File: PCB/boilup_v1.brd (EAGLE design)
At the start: 46.7 x 80 mm, 38 parts, among them IC1 THS4211, J1 USB-MICROB, U1 STM32F0_LQFP64, U2 SPX3819-3.3

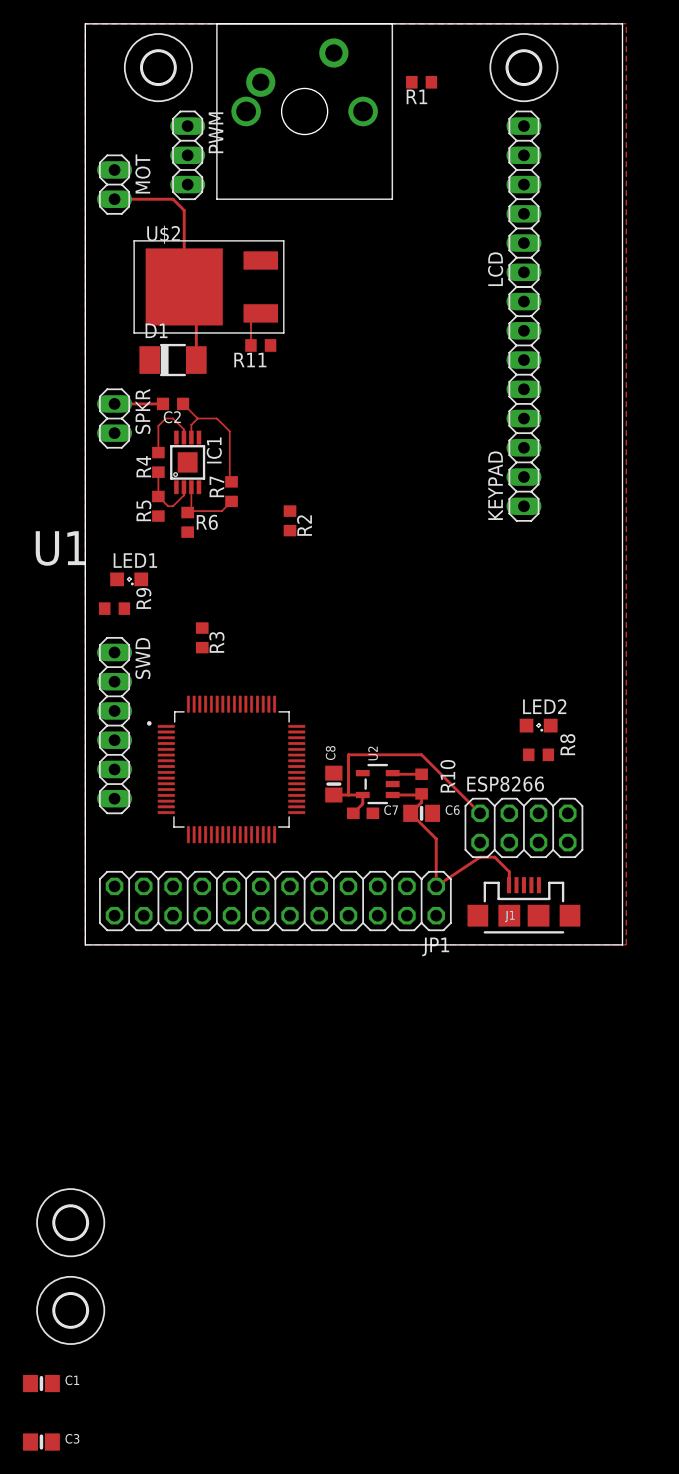
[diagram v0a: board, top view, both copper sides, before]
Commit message: Initial routing + pinout
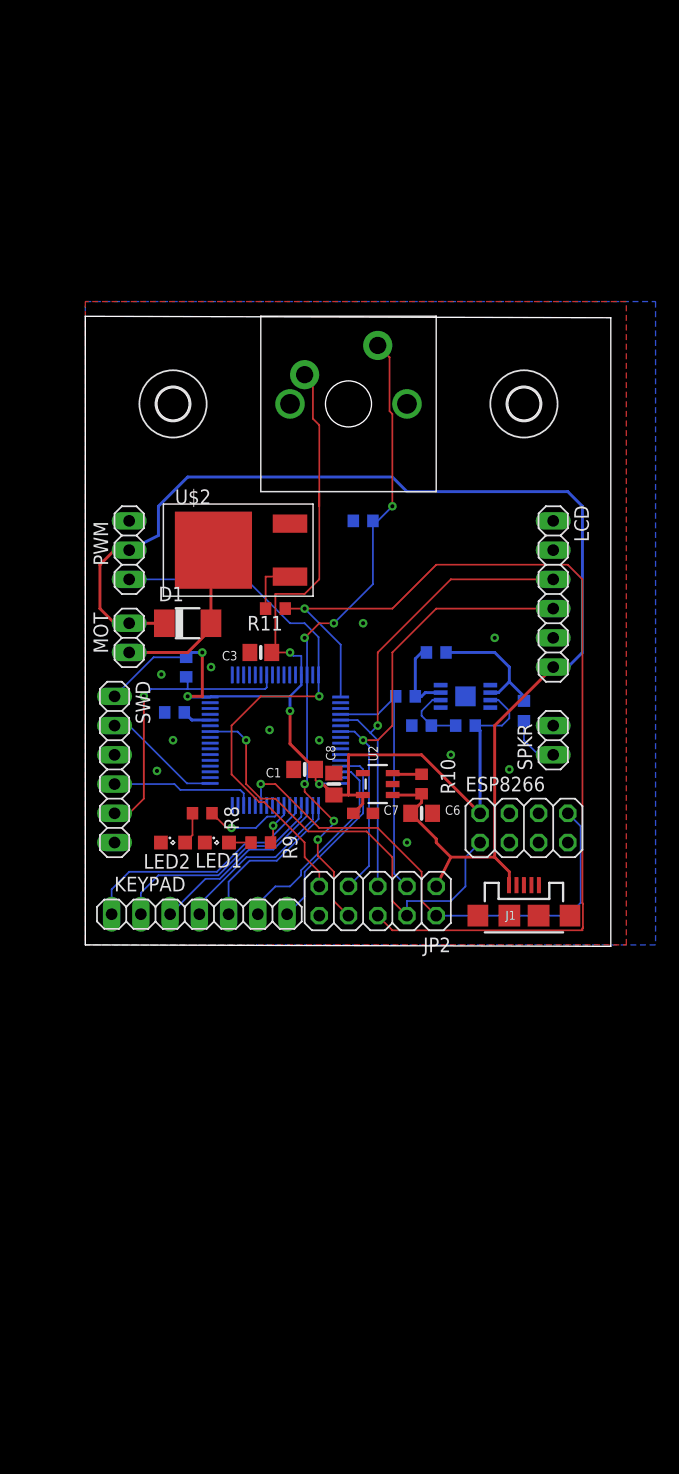
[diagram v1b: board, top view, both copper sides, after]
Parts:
- removed H3, H4: MOUNT-HOLE2.8, holes:2,8
- removed JP1: (no value), pinhead:2X12
- added JP2: (no value), pinhead:2X05
- KEYPAD: device pinhead:1X08 -> pinhead:1X07
- moved C3 71.2 mm to (15.2, 25.4), turned to 180 degrees
- moved C1 58.0 mm to (19.1, 15.2), turned to 180 degrees
- moved KEYPAD 52.5 mm to (9.91, 2.67), turned to 180 degrees
- moved SPKR 47.2 mm to (40.6, 17.8), turned to 90 degrees
- moved C2 40.5 mm to (38.1, 20.3), flipped to the bottom, turned to 270 degrees
- moved MOT 39.4 mm to (3.81, 26.7)
- moved R1 38.4 mm to (24.1, 36.8), flipped to the bottom
- moved R4 35.1 mm to (33.0, 19.1), flipped to the bottom, turned to 0 degrees
- moved PWM 34.7 mm to (3.81, 34.3)
- moved LCD 34.4 mm to (40.6, 30.5), turned to 270 degrees
- moved LED2 33.3 mm to (7.62, 8.89), turned to 0 degrees
- moved IC1 31.5 mm to (33.0, 21.6), flipped to the bottom, turned to 90 degrees
- moved R5 29.8 mm to (29.2, 19.1), flipped to the bottom, turned to 0 degrees
- moved R8 29.6 mm to (10.2, 11.4)
- moved H2 29.2 mm to (7.62, 47.0)
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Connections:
- removed net KETTLESWITCH: R1.2, U$1.SW2
- removed net N$22: JP1.22
- removed net N$23: JP1.20
- net +5V: now also JP2.1; no longer JP1.1
- net COL1: no longer JP1.11
- net COL2: no longer JP1.13
- net COL3: no longer JP1.15
- net DAC: now also JP2.3; no longer JP1.17
- net GND: now also JP2.10; no longer JP1.24
- net LED3: no longer JP1.12
- net LED4: no longer JP1.14
- net MISO: no longer JP1.21
- net MOSI: now also JP2.7; no longer JP1.23
- net PUSH_BUTT: now also JP2.8, R1.2, U$1.SW2; no longer JP1.10
- net ROW1: no longer JP1.3
- net ROW2: no longer JP1.5
- net ROW3: no longer JP1.7
- net ROW4: no longer JP1.9
- net SCK: now also JP2.5; no longer JP1.19
- net SWCLK: no longer JP1.18
- net SWDIO: no longer JP1.16
- net TIM2_CH3: now also JP2.9; no longer JP1.6
- net TIM2_CH4: now also JP2.6; no longer JP1.8
- net USART_RX: now also JP2.2; no longer JP1.2
- net USART_TX: now also JP2.4; no longer JP1.4
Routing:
- net +5V: track 20.7 -> 111.2 mm
- net TIM2_CH4: track 0.00 -> 85.7 mm, vias 0 -> 1
- net +3V3: track 27.4 -> 106.3 mm, vias 0 -> 5
- net PUSH_BUTT: track 0.00 -> 57.1 mm, vias 0 -> 6
- net TIM2_CH3: track 0.00 -> 49.7 mm, vias 0 -> 1
- net USART_RX: track 0.00 -> 44.6 mm, vias 0 -> 1
- net SCK: track 0.00 -> 41.8 mm, vias 0 -> 1
- net MOSI: track 0.00 -> 41.3 mm, vias 0 -> 1
- net USART_TX: track 0.00 -> 39.4 mm, vias 0 -> 1
- net NRST: track 0.00 -> 25.1 mm, vias 0 -> 1
- net DAC: track 0.00 -> 22.3 mm
- net COL3: track 0.00 -> 21.7 mm
- net COL2: track 0.00 -> 19.5 mm
- net ROW2: track 0.00 -> 18.0 mm
- net ROW1: track 0.00 -> 17.4 mm
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- added copper zone on layer 16, net GND
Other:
- board size 46.7 x 80 mm -> 45.6 x 54.7 mm

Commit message: Updated CAD and PCB
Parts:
- moved LCD 11.5 mm to (41.9, 41.9), turned to 90 degrees
- moved H2 2.54 mm to (10.2, 47.0)
- moved H1 2.54 mm to (35.6, 47.0)
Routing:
- net +5V: track 111.2 -> 132.9 mm, vias 0 -> 1
- net MOSI: track 41.3 -> 50.2 mm, vias 1 -> 2
- net SCK: track 41.8 -> 47.2 mm
- net TIM2_CH4: track 85.7 -> 83.1 mm, vias 1 -> 3
